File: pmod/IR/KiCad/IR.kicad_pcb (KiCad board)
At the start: 2 copper layers, 25.4 x 15.2 mm, 8 parts, among them J1 Conn_02x06_Odd_Even, Q1 BC337, Q2 BC327

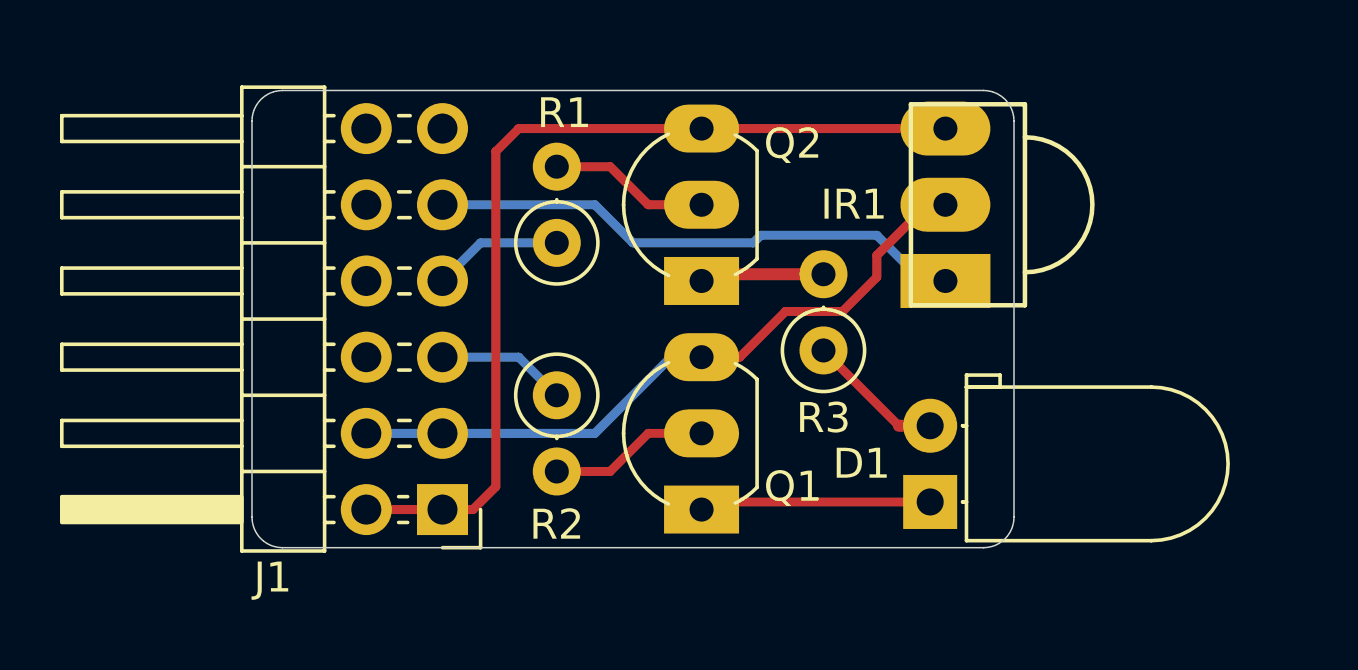
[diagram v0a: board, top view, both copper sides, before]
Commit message: Update IR module
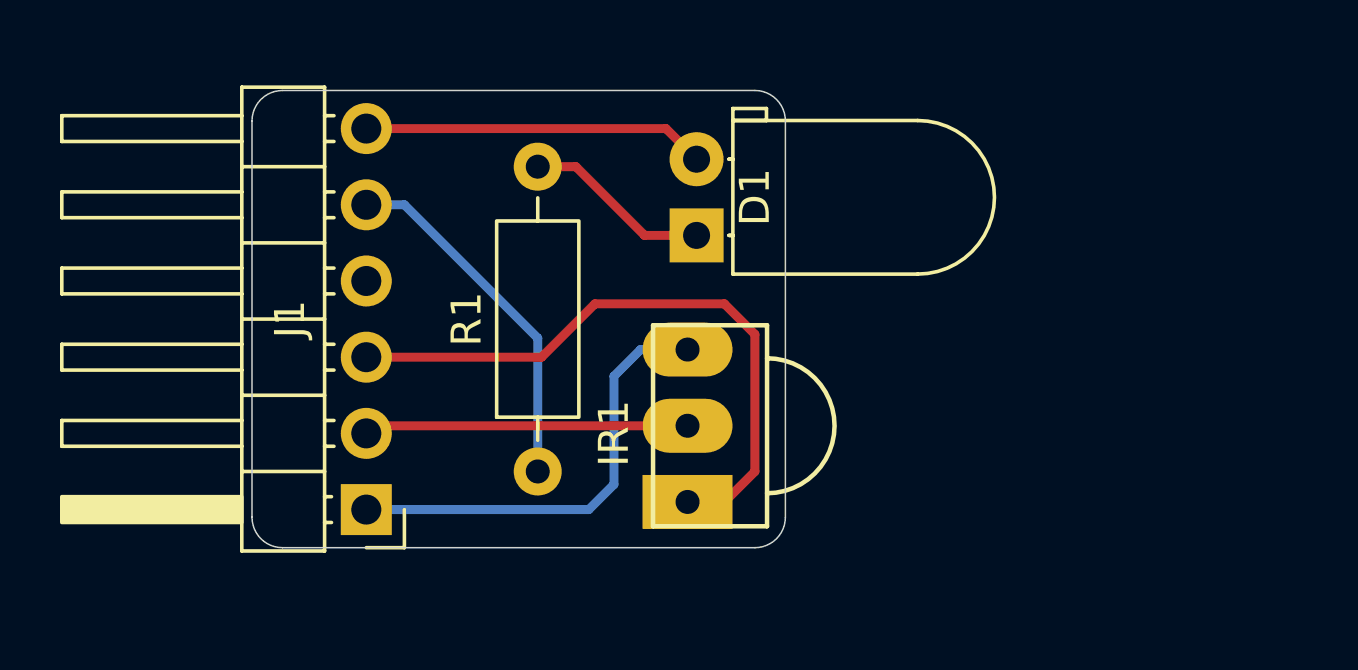
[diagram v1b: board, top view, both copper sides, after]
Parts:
- removed Q1: BC337, Package_TO_SOT_THT:TO-92_Inline_Wide
- removed Q2: BC327, Package_TO_SOT_THT:TO-92_Inline_Wide
- removed R2: 220, Resistor_THT:R_Axial_DIN0207_L6.3mm_D2.5mm_P2.54mm_Vertical
- removed R3: 67, Resistor_THT:R_Axial_DIN0207_L6.3mm_D2.5mm_P2.54mm_Vertical
- J1: value Conn_02x06_Odd_Even -> Conn_01x06; footprint Connector_PinHeader_2.54mm:PinHeader_2x06_P2.54mm_Horizontal -> Connector_PinHeader_2.54mm:PinHeader_1x06_P2.54mm_Horizontal
- R1: value 220 -> 180; footprint Resistor_THT:R_Axial_DIN0207_L6.3mm_D2.5mm_P2.54mm_Vertical -> Resistor_THT:R_Axial_DIN0207_L6.3mm_D2.5mm_P10.16mm_Horizontal
- moved D1 11.8 mm to (85.9, 48.0)
- moved IR1 11.3 mm to (85.6, 54.4)
- moved R1 7.65 mm to (80.6, 55.9)
- moved J1 2.54 mm to (74.9, 57.1)
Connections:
- D1 pad 2: Net-(D1-A) -> CLK
- J1 pad 2: +3.3V -> GND
- J1 pad 3: GND -> RX
- J1 pad 4: GND -> unconnected-(J1-Pin_4-Pad4)
- J1 pad 5: CLK -> TX
- J1 pad 6: unconnected-(J1-Pin_6-Pad6) -> CLK
- R1 pad 2: Net-(Q2-B) -> Net-(D1-K)
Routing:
- net +3.3V: track 32.1 -> 15.0 mm
- net GND: track 22.9 -> 10.8 mm
- net TX: track 4.34 -> 12.0 mm
- net CLK: track 4.34 -> 11.4 mm
- net Net-(Q2-B): track 5.35 -> 0.00 mm
- net Net-(Q1-B): track 5.35 -> 0.00 mm
- net RX: track 18.0 -> 22.7 mm
- net Net-(D1-A): track 4.60 -> 0.00 mm
- net Net-(Q2-C): track 4.16 -> 0.00 mm
- net Net-(D1-K): track 7.73 -> 6.96 mm
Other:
- board size 25.4 x 15.2 mm -> 17.8 x 15.2 mm

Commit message: Board V2
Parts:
- moved R1 10.2 mm to (80.3, 45.7), turned to 0 degrees
- moved IR1 10.2 mm to (95.8, 54.4)
- moved D1 10.1 mm to (96.0, 48.0)
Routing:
- net GND: track 10.8 -> 21.8 mm, vias 0 -> 1
- net CLK: track 11.4 -> 21.9 mm
- net +3.3V: track 15.0 -> 23.6 mm
- net TX: track 12.0 -> 5.86 mm
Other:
- board size 17.8 x 15.2 mm -> 26.9 x 15.2 mm
- board text added: "IR"
- board text added: "IR Modul"
- board text added: "pmod.robotikabrno.cz/"

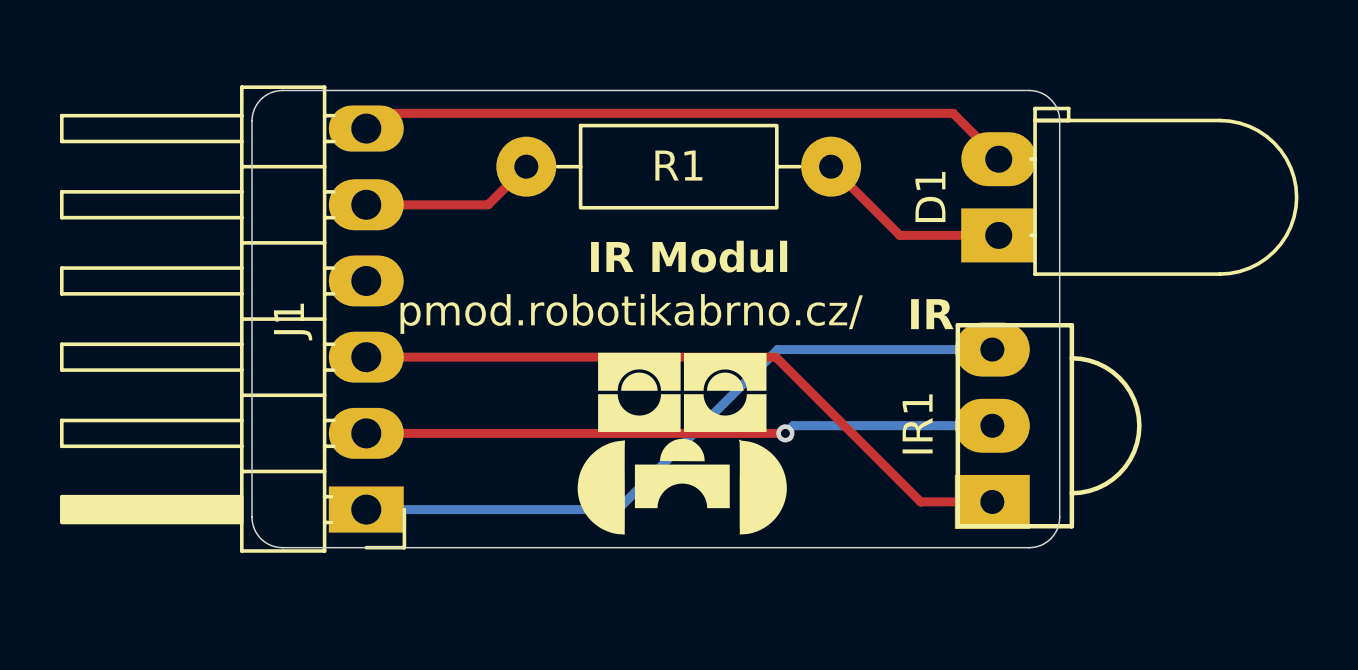
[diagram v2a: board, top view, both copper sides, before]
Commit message: Add Mounting hole
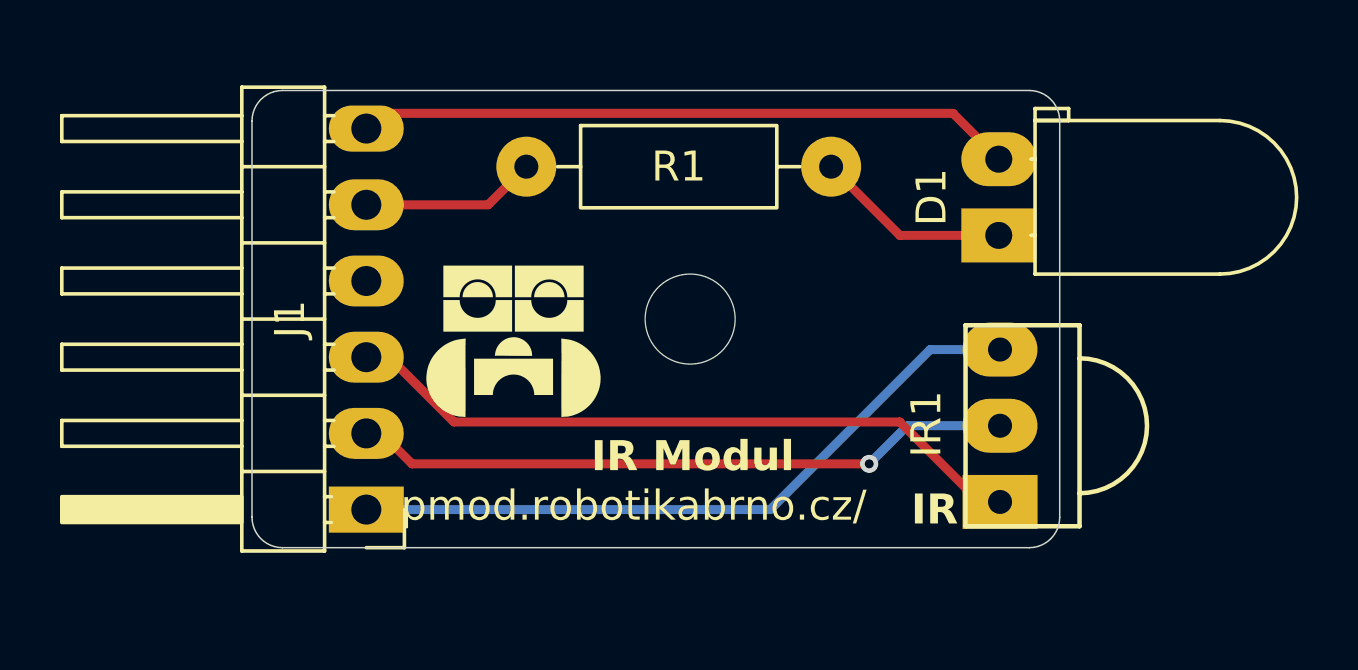
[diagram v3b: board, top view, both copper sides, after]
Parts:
- added REF**: MountingHole_3mm, MountingHole:MountingHole_3mm, F.Cu at (85.7, 50.8)
- moved IR1 0.26 mm to (96.1, 54.4)
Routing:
- net GND: track 21.8 -> 22.9 mm

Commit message: fix: small pcb fixes
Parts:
- removed REF**: MountingHole_3mm, MountingHole:MountingHole_3mm
- added M3: MountingHole_3.2mm_M3, MountingHole:MountingHole_3.2mm_M3, F.Cu at (86.4, 50.8)
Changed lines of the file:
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@@
 		)
-	)
-	(footprint "MountingHole:MountingHole_3mm"
-		(layer "F.Cu")
-		(at 85.725 50.8)
-		(descr "Mounting Hole 3mm, no annular, generated by kicad-footprint-generator mountinghole.py")
-		(tags "mountinghole")
-		(property "Reference" "REF**"
-			(at 0 -3.95 0)
-			(layer "F.SilkS")
-			(hide yes)
-			(effects
-				(font
-					(size 1 1)
-					(thickness 0.15)
-				)
-			)
-		)
-		(property "Value" "MountingHole_3mm"
-			(at 0 3.95 0)
-			(layer "F.Fab")
-			(hide yes)
-			(effects
-				(font
-					(size 1 1)
-					(thickness 0.15)
-				)
-			)
-		)
-		(property "Datasheet" ""
-			(at 0 0 0)
-			(layer "F.Fab")
-			(hide yes)
-			(effects
-				(font
-					(size 1.27 1.27)
-					(thickness 0.15)
-				)
-			)
-		)
-		(property "Description" ""
-			(at 0 0 0)
-			(layer "F.Fab")
-			(hide yes)
-			(effects
-				(font
-					(size 1.27 1.27)
-					(thickness 0.15)
-				)
-			)
-		)
-		(attr exclude_from_pos_files exclude_from_bom)
-		(fp_circle
-			(center 0 0)
-			(end 3 0)
-			(stroke
-				(width 0.15)
-				(type solid)
-			)
-			(fill no)
-			(layer "Cmts.User")
-		)
-		(fp_circle
-			(center 0 0)
-			(end 3.25 0)
-			(stroke
-				(width 0.05)
-				(type solid)
-			)
-			(fill no)
-			(layer "F.CrtYd")
-		)
-		(fp_text user "${REFERENCE}"
-			(at 0 0 0)
-			(layer "F.Fab")
-			(effects
-				(font
-					(size 1 1)
-					(thickness 0.15)
-				)
-			)
-		)
-		(pad "" np_thru_hole circle
-			(at 0 0)
-			(size 3 3)
-			(drill 3)
-			(layers "*.Cu" "*.Mask")
-		)
-		(embedded_fonts no)
 	)
 	(footprint "Connector_PinHeader_2.54mm:PinHeader_1x06_P2.54mm_Horizontal"
@@
 		)
 	)
+	(footprint "MountingHole:MountingHole_3.2mm_M3"
+		(layer "F.Cu")
+		(at 86.36 50.8)
+		(descr "Mounting Hole 3.2mm, M3, no annular, generated by kicad-footprint-generator mountinghole.py")
+		(tags "mountinghole M3")
+		(property "Reference" "M3"
+			(at 3.048 0 90)
+			(layer "F.SilkS")
+			(effects
+				(font
+					(size 1 1)
+					(thickness 0.15)
+				)
+			)
+		)
+		(property "Value" "MountingHole_3.2mm_M3"
+			(at 0 4.15 0)
+			(layer "F.Fab")
+			(hide yes)
+			(effects
+				(font
+					(size 1 1)
+					(thickness 0.15)
+				)
+			)
+		)
+		(property "Datasheet" ""
+			(at 0 0 0)
+			(layer "F.Fab")
+			(hide yes)
+			(effects
+				(font
+					(size 1.27 1.27)
+					(thickness 0.15)
+				)
+			)
+		)
+		(property "Description" ""
+			(at 0 0 0)
+			(layer "F.Fab")
+			(hide yes)
+			(effects
+				(font
+					(size 1.27 1.27)
+					(thickness 0.15)
+				)
+			)
+		)
+		(attr exclude_from_pos_files exclude_from_bom)
+		(fp_circle
+			(center 0 0)
+			(end 3.2 0)
+			(stroke
+				(width 0.15)
+				(type solid)
+			)
+			(fill no)
+			(layer "Cmts.User")
+		)
+		(fp_circle
+			(center 0 0)
+			(end 3.45 0)
+			(stroke
+				(width 0.05)
+				(type solid)
+			)
+			(fill no)
+			(layer "F.CrtYd")
+		)
+		(fp_text user "${REFERENCE}"
+			(at 0 0 0)
+			(layer "F.Fab")
+			(effects
+				(font
+					(size 1 1)
+					(thickness 0.15)
+				)
+			)
+		)
+		(pad "" np_thru_hole circle
+			(at 0 0)
+			(size 3.2 3.2)
+			(drill 3.2)
+			(layers "*.Cu" "*.Mask")
+		)
+		(embedded_fonts no)
+	)
 	(gr_poly

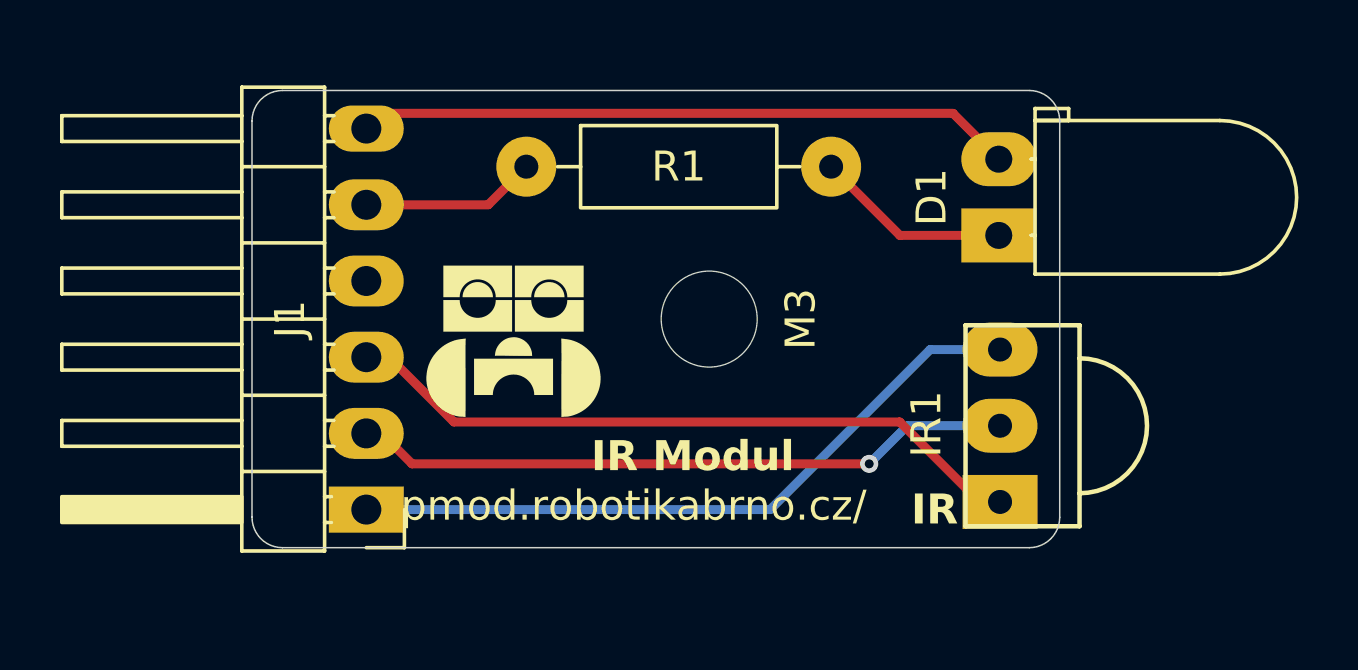
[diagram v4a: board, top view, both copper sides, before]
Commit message: fix: add copper fill to IR pcb
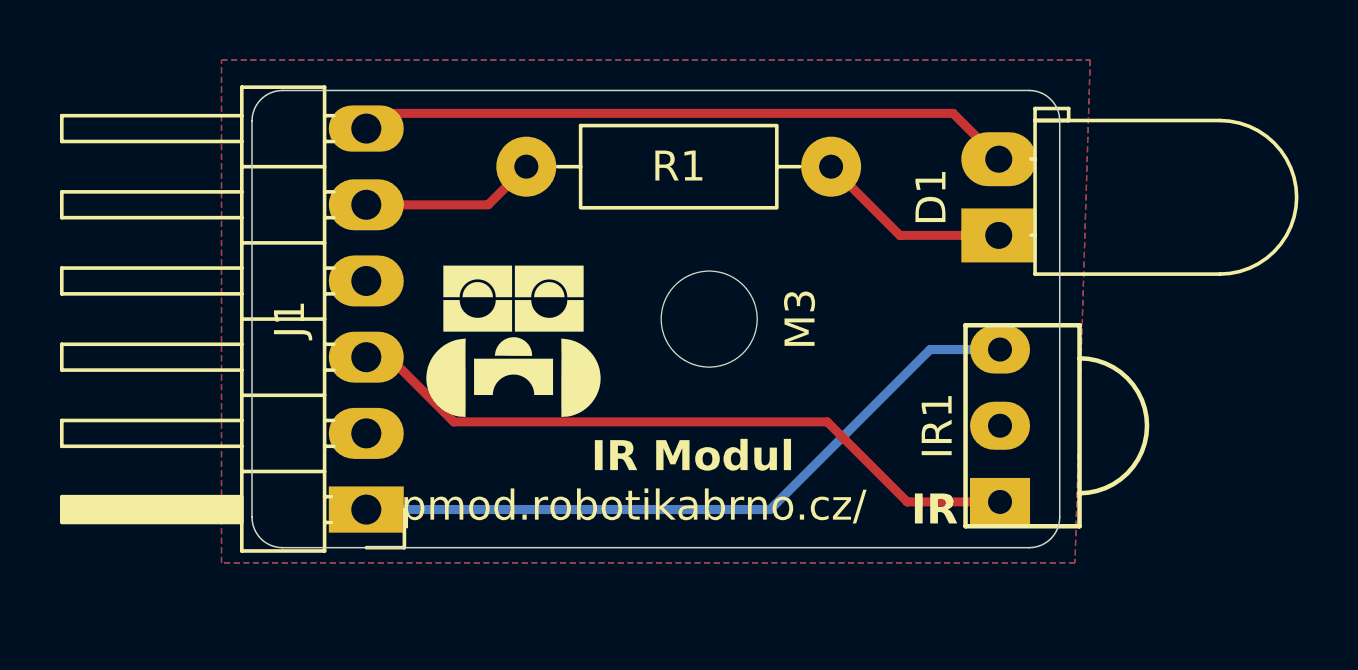
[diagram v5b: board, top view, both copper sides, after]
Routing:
- net GND: track 22.9 -> 1.37 mm, vias 1 -> 0
- added copper zone on B.Cu, net GND
- added copper zone on F.Cu, net GND
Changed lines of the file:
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@@
 		(at 96.0545 54.356 180)
 		(property "Reference" "IR1"
-			(at 2.4535 0.056 90)
+			(at 2.0745 0 90)
 			(layer "F.SilkS")
 			(effects
@@
 		(pad "1" thru_hole rect
 			(at 0 -2.54 180)
-			(size 2.5 1.8)
+			(size 2 1.6)
 			(drill 0.8)
 			(layers "*.Cu" "*.Mask")
@@
 		(pad "2" thru_hole oval
 			(at 0 0 180)
-			(size 2.5 1.8)
+			(size 2 1.6)
 			(drill 0.8)
 			(layers "*.Cu" "*.Mask")
@@
 		(pad "3" thru_hole oval
 			(at 0 2.54 180)
-			(size 2.5 1.8)
+			(size 2 1.6)
 			(drill 0.8)
 			(layers "*.Cu" "*.Mask")
@@
 	)
 	(segment
-		(start 76.454 55.626)
-		(end 75.438 54.61)
-		(width 0.3)
-		(layer "F.Cu")
-		(net 2)
-	)
-	(segment
-		(start 91.694 55.626)
-		(end 76.454 55.626)
+		(start 74.93 52.07)
+		(end 75.692 52.07)
 		(width 0.3)
 		(layer "F.Cu")
-		(net 2)
-	)
-	(via
-		(at 91.694 55.626)
-		(size 0.6)
-		(drill 0.3)
-		(layers "F.Cu" "B.Cu")
-		(net 2)
-	)
-	(segment
-		(start 92.964 54.356)
-		(end 96.0545 54.356)
-		(width 0.3)
-		(layer "B.Cu")
-		(net 2)
-	)
-	(segment
-		(start 91.694 55.626)
-		(end 92.964 54.356)
-		(width 0.3)
-		(layer "B.Cu")
-		(net 2)
+		(net 3)
 	)
 	(segment
 		(start 77.851 54.229)
-		(end 92.71 54.229)
+		(end 90.297 54.229)
 		(width 0.3)
 		(layer "F.Cu")
@@
 	)
 	(segment
-		(start 74.93 52.07)
-		(end 75.692 52.07)
+		(start 92.964 56.896)
+		(end 96.0545 56.896)
 		(width 0.3)
 		(layer "F.Cu")
@@
 	)
 	(segment
-		(start 95.377 56.896)
-		(end 96.0545 56.896)
-		(width 0.3)
-		(layer "F.Cu")
-		(net 3)
-	)
-	(segment
-		(start 92.71 54.229)
-		(end 95.377 56.896)
+		(start 90.297 54.229)
+		(end 92.964 56.896)
 		(width 0.3)
 		(layer "F.Cu")
@@
 		(net 7)
 	)
+	(zone
+		(net 2)
+		(net_name "GND")
+		(layers "F.Cu" "B.Cu")
+		(hatch edge 0.5)
+		(connect_pads
+			(clearance 0.25)
+		)
+		(min_thickness 0.25)
+		(filled_areas_thickness no)
+		(fill yes
+			(thermal_gap 0.25)
+			(thermal_bridge_width 0.5)
+		)
+		(polygon
+			(pts
+				(xy 70.104 42.164) (xy 99.06 42.164) (xy 98.552 58.928) (xy 70.104 58.928)
+			)
+		)
+	)
 	(group ""
